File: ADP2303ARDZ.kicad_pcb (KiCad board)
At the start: 2 copper layers, 28 x 38 mm, 16 parts, among them P1 CONN_01X03, P2 CONN_01X03, U1 ADP230x, U2 MCP1825S

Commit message: rough layout
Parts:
- removed G***: LOGO, electronicSoup:LOGO
- added R2: R, footprints:R_0603_1608Metric, F.Cu at (144.6, 115.2)
- added R3: R, footprints:R_0603_1608Metric, F.Cu at (148.0, 115.2)
- C1, C2, C4, C6, C7: footprint Capacitors_SMD:C_0603_HandSoldering -> footprints:C_0603_1608Metric
- C3: value 0.1uF -> 0,1uF; footprint Capacitors_SMD:C_0603_HandSoldering -> footprints:C_0603_1608Metric
- C5: value C_Small -> C; footprint Capacitors_SMD:C_0603_HandSoldering -> footprints:C_0603_1608Metric
- D1: footprint Diodes_SMD:SMB_Standard -> footprints:D_SMB_Handsoldering
- L1: value 4.7uH -> VLF10040T; footprint electronicSoup:Inductor-VLF10040 -> footprints:L_TDK_VLF10040
- L2: value 3uH -> SRN6028; footprint electronicSoup:Inductor-SRN6028-Series -> footprints:L_Bourns-SRN6028
- P1: value CONN_01X03 -> Input; footprint Pin_Headers:Pin_Header_Straight_1x03 -> footprints:PinSocket_1x03_P2.54mm_Vertical
- P2: value CONN_01X03 -> Output; footprint Pin_Headers:Pin_Header_Straight_1x03 -> footprints:PinSocket_1x03_P2.54mm_Vertical
- R1: footprint Resistors_SMD:R_0603_HandSoldering -> footprints:R_0603_1608Metric
- U1: value ADP230x -> ADP2303ARDZ-5.0; footprint Housings_SOIC:SOIC-8-1EP_3.9x4.9mm_Pitch1.27mm -> footprints:SOIC-8-1EP_3.9x4.9mm_Pitch1.27mm
- U2: footprint TO_SOT_Packages_SMD:SOT-223 -> footprints:SOT-223
- moved L2 0.36 mm to (145.2, 83.9), turned to 0 degrees
- turned C1 to 90 degrees
- turned C2 to 90 degrees
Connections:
- net /3v3 renamed Net-(C7-Pad1)
- net /BST renamed Net-(C3-Pad1)
- net /SW renamed Net-(C3-Pad2)
- C1 pad 1: /Gnd -> Net-(C1-Pad1)
- C1 pad 2: /Vin -> Net-(C1-Pad2)
- C2 pad 1: /Gnd -> Net-(C1-Pad1)
- C2 pad 2: /Vin -> Net-(C1-Pad2)
- C4 pad 1: /5V -> Net-(C4-Pad1)
- C4 pad 2: /Gnd -> Net-(C1-Pad2)
- C5 pad 1: /5V -> Net-(C4-Pad1)
- C5 pad 2: /Gnd -> Net-(C1-Pad2)
- C6 pad 1: /5V -> Net-(C4-Pad1)
- C6 pad 2: /Gnd -> Net-(C1-Pad2)
- C7 pad 2: /Gnd -> Net-(C1-Pad2)
- D1 pad 2: /Gnd -> Net-(C1-Pad2)
- L1 pad 2: /5V -> Net-(C4-Pad1)
- L2 pad 2: /5V -> Net-(C4-Pad1)
- P1 pad 1: /Gnd -> Net-(C1-Pad2)
- P1 pad 2: /Vin -> Net-(C1-Pad1)
- P1 pad 3: /Gnd -> Net-(C1-Pad2)
- P2 pad 1: /Gnd -> Net-(C4-Pad1)
- P2 pad 3: /5V -> Net-(C1-Pad2)
- R1 pad 1: /Vin -> Net-(C1-Pad1)
- U1 pad 2: /Vin -> Net-(C1-Pad1)
- U1 pad 3: /Vin -> Net-(C1-Pad1)
- U1 pad 5: /5V -> Net-(R2-Pad1)
- U1 pad 6: (no net) -> Net-(U1-Pad6)
- U1 pad 7: /Gnd -> Net-(C1-Pad2)
- U1 pad 9: /Gnd -> Net-(C1-Pad2)
- U2 pad 1: /5V -> Net-(C4-Pad1)
- U2 pad 2: /Gnd -> Net-(C1-Pad2)
- U2 pad 4: /Gnd -> (no net)
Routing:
- net /Gnd: track 110.8 -> 0.00 mm
- net /5V: track 79.1 -> 0.00 mm, vias 1 -> 0
- net Net-(C3-Pad2): track 38.5 -> 3.32 mm
- net /Vin: track 19.9 -> 0.00 mm
- added copper zone on F.Cu, net /SW
- removed copper zone on B.Cu, net /Gnd
- removed copper zone on F.Cu, net Net-(C3-Pad2)

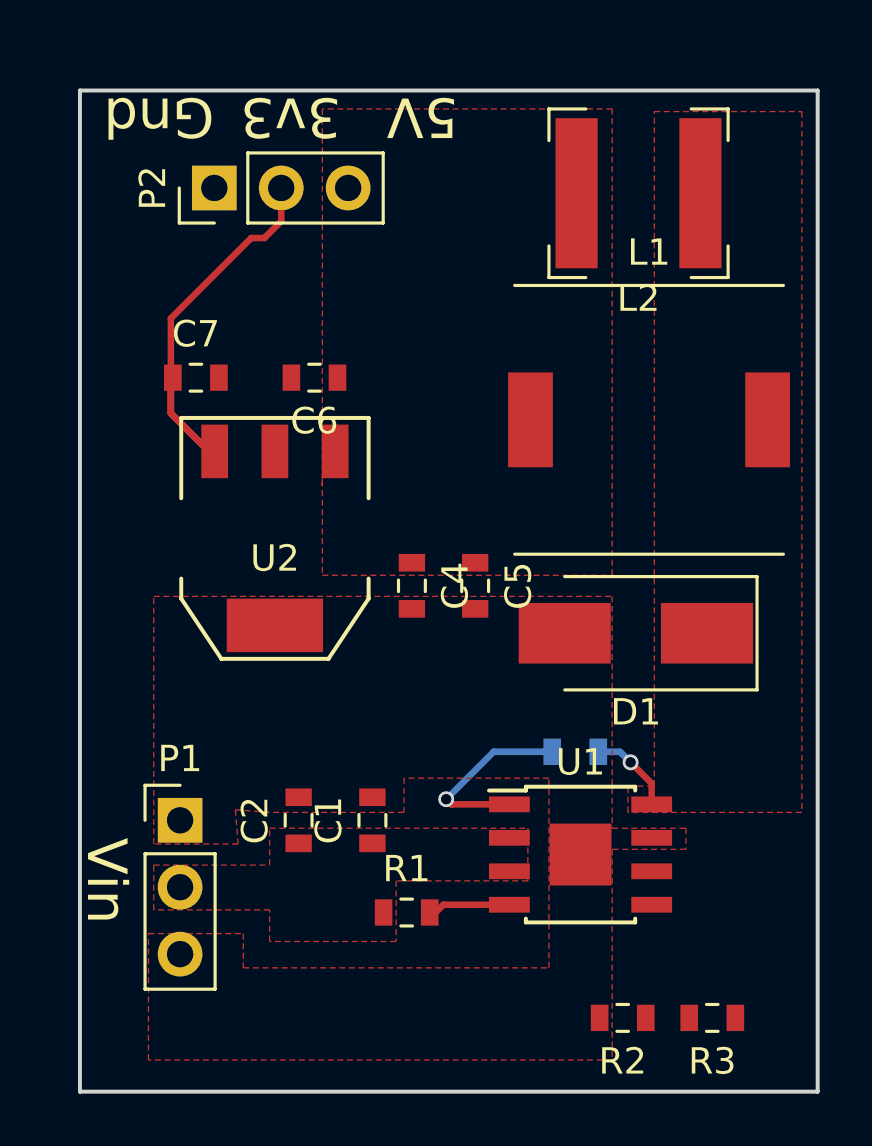
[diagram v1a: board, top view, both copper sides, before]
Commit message: corrected orientation of Inductors
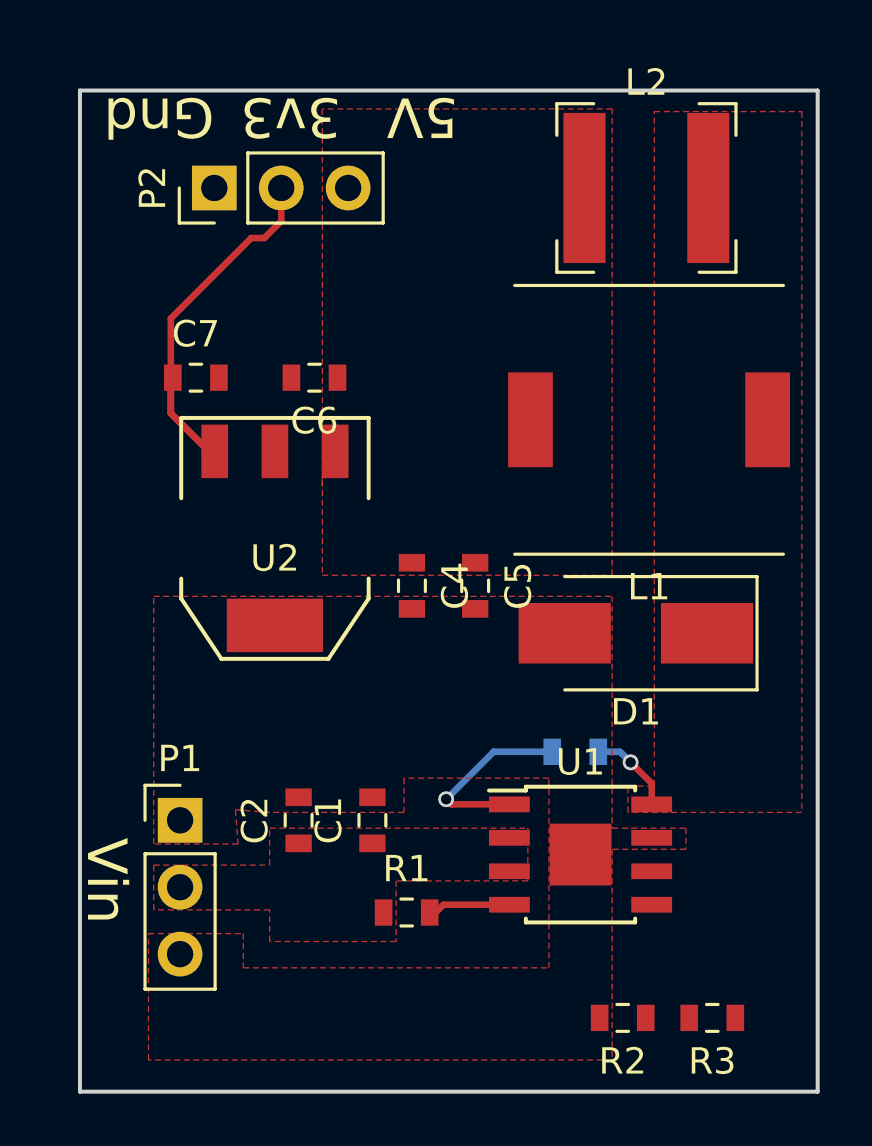
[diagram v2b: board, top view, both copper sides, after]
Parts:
- moved L2 0.36 mm to (145.5, 83.7), turned to 180 degrees
- turned L1 to 180 degrees
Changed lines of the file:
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@@
   )
   (module footprints:L_TDK_VLF10040 (layer F.Cu)
-    (at 145.6 92.5)
+    (at 145.6 92.5 180)
     (descr "Inductor,TDK, TDK-VLP-8040, 8.6mmx8.6mm")
     (tags "inductor TDK VLP smd VLF10040")
     (attr smd)
-    (fp_text reference L1 (at 0 -6.35) (layer F.SilkS)
+    (fp_text reference L1 (at 0 -6.35 180) (layer F.SilkS)
       (effects (font (size 1 1) (thickness 0.15)))
     )
-    (fp_text value VLF10040T (at 0 6) (layer F.Fab)
+    (fp_text value VLF10040T (at 0 6 180) (layer F.Fab)
       (effects (font (size 1 1) (thickness 0.15)))
     )
-    (fp_text user %R (at 0 0) (layer F.Fab)
+    (fp_text user %R (at 0 0 180) (layer F.Fab)
       (effects (font (size 1 1) (thickness 0.15)))
     )
@@
     (fp_line (start -5.1 -5.1) (end 5.1 -5.1) (layer F.SilkS) (width 0.12))
     (fp_circle (center 0 0) (end 3 3) (layer F.Fab) (width 0.1))
-    (pad 1 smd rect (at -4.5 0) (size 1.7 3.6) (layers F.Cu F.Paste F.Mask)
+    (pad 1 smd rect (at -4.5 0 180) (size 1.7 3.6) (layers F.Cu F.Paste F.Mask)
       (net 9 "Net-(C3-Pad2)"))
-    (pad 2 smd rect (at 4.5 0) (size 1.7 3.6) (layers F.Cu F.Paste F.Mask)
+    (pad 2 smd rect (at 4.5 0 180) (size 1.7 3.6) (layers F.Cu F.Paste F.Mask)
       (net 10 "Net-(C4-Pad1)"))
     (model ${KISYS3DMOD}/Inductor_SMD.3dshapes/L_TDK_VLF10040.wrl
@@
   )
   (module footprints:L_Bourns-SRN6028 (layer F.Cu)
-    (at 145.2 83.9)
+    (at 145.5 83.7 180)
     (descr "Bourns SRN6028 series SMD inductor")
     (tags "Bourns SRN6028 SMD inductor")
     (attr smd)
-    (fp_text reference L2 (at 0 4) (layer F.SilkS)
+    (fp_text reference L2 (at 0 4 180) (layer F.SilkS)
       (effects (font (size 1 1) (thickness 0.15)))
     )
-    (fp_text value SRN6028 (at 0 -4) (layer F.Fab)
+    (fp_text value SRN6028 (at 0 -4 180) (layer F.Fab)
       (effects (font (size 1 1) (thickness 0.15)))
     )
-    (fp_text user %R (at 0 0) (layer F.Fab)
+    (fp_text user %R (at 0 0 180) (layer F.Fab)
       (effects (font (size 1 1) (thickness 0.15)))
     )
@@
     (fp_line (start 3.3 3.1) (end -3.3 3.1) (layer F.CrtYd) (width 0.05))
     (fp_line (start -3.3 -3.1) (end -3.3 3.1) (layer F.CrtYd) (width 0.05))
-    (pad 1 smd rect (at -2.35 0) (size 1.6 5.7) (layers F.Cu F.Paste F.Mask)
+    (pad 1 smd rect (at -2.35 0 180) (size 1.6 5.7) (layers F.Cu F.Paste F.Mask)
       (net 9 "Net-(C3-Pad2)"))
-    (pad 2 smd rect (at 2.35 0) (size 1.6 5.7) (layers F.Cu F.Paste F.Mask)
+    (pad 2 smd rect (at 2.35 0 180) (size 1.6 5.7) (layers F.Cu F.Paste F.Mask)
       (net 10 "Net-(C4-Pad1)"))
     (model ${KISYS3DMOD}/Inductor_SMD.3dshapes/L_Bourns-SRN6028.wrl

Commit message: Fully connected but no Gnd plane as yet
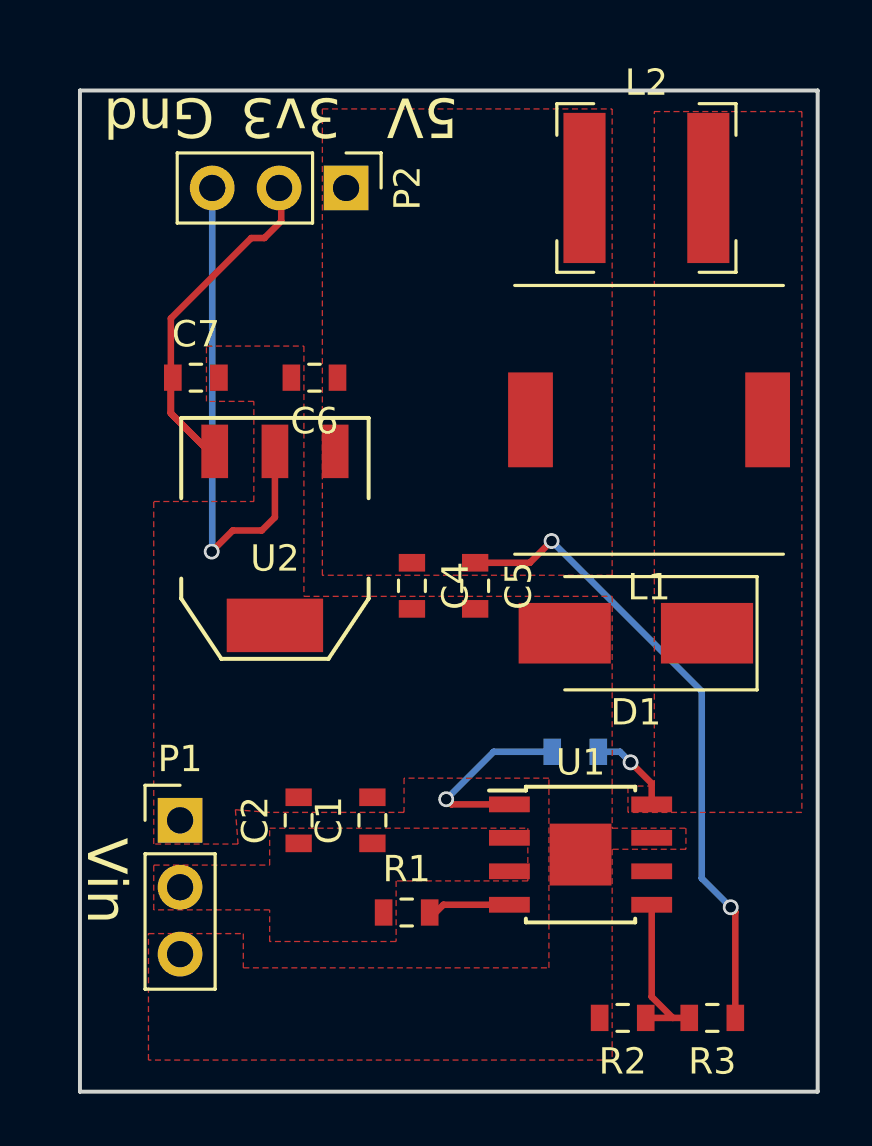
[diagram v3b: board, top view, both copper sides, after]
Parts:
- moved P2 5.00 mm to (134.1, 83.7), turned to 270 degrees
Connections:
- net Net-(C4-Pad1) renamed /5v
- net Net-(C7-Pad1) renamed /3v3
- C1 pad 1: Net-(C1-Pad1) -> /Vin
- C1 pad 2: Net-(C1-Pad2) -> /Gnd
- C2 pad 1: Net-(C1-Pad1) -> /Vin
- C2 pad 2: Net-(C1-Pad2) -> /Gnd
- C3 pad 2: Net-(C3-Pad2) -> /SW
- C4 pad 2: Net-(C1-Pad2) -> /Gnd
- C5 pad 2: Net-(C1-Pad2) -> /Gnd
- C6 pad 2: Net-(C1-Pad2) -> /Gnd
- C7 pad 2: Net-(C1-Pad2) -> /Gnd
- D1 pad 1: Net-(C3-Pad2) -> /SW
- D1 pad 2: Net-(C1-Pad2) -> /Gnd
- L1 pad 1: Net-(C3-Pad2) -> /SW
- L2 pad 1: Net-(C3-Pad2) -> /SW
- P1 pad 1: Net-(C1-Pad2) -> /Gnd
- P1 pad 2: Net-(C1-Pad1) -> /Vin
- P1 pad 3: Net-(C1-Pad2) -> /Gnd
- P2 pad 3: Net-(C1-Pad2) -> /Gnd
- R1 pad 1: Net-(C1-Pad1) -> /Vin
- R2 pad 2: Net-(C1-Pad2) -> /Gnd
- U1 pad 2: Net-(C1-Pad1) -> /Vin
- U1 pad 3: Net-(C1-Pad1) -> /Vin
- U1 pad 6: Net-(U1-Pad6) -> (no net)
- U1 pad 7: Net-(C1-Pad2) -> /Gnd
- U1 pad 8: Net-(C3-Pad2) -> /SW
- U1 pad 9: Net-(C1-Pad2) -> /Gnd
- U2 pad 2: Net-(C1-Pad2) -> /Gnd
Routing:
- net /5v: track 0.00 -> 24.2 mm, vias 0 -> 2
- net /Gnd: track 0.00 -> 19.2 mm, vias 0 -> 1
- net Net-(R2-Pad1): track 0.00 -> 6.28 mm
- net Net-(C3-Pad2): track 3.32 -> 0.00 mm, vias 1 -> 0
- net /SW: track 0.00 -> 3.32 mm, vias 0 -> 1
- added copper zone on F.Cu, net /5v
- removed copper zone on F.Cu, net /5V

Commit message: Added 0805 Cap Footprint
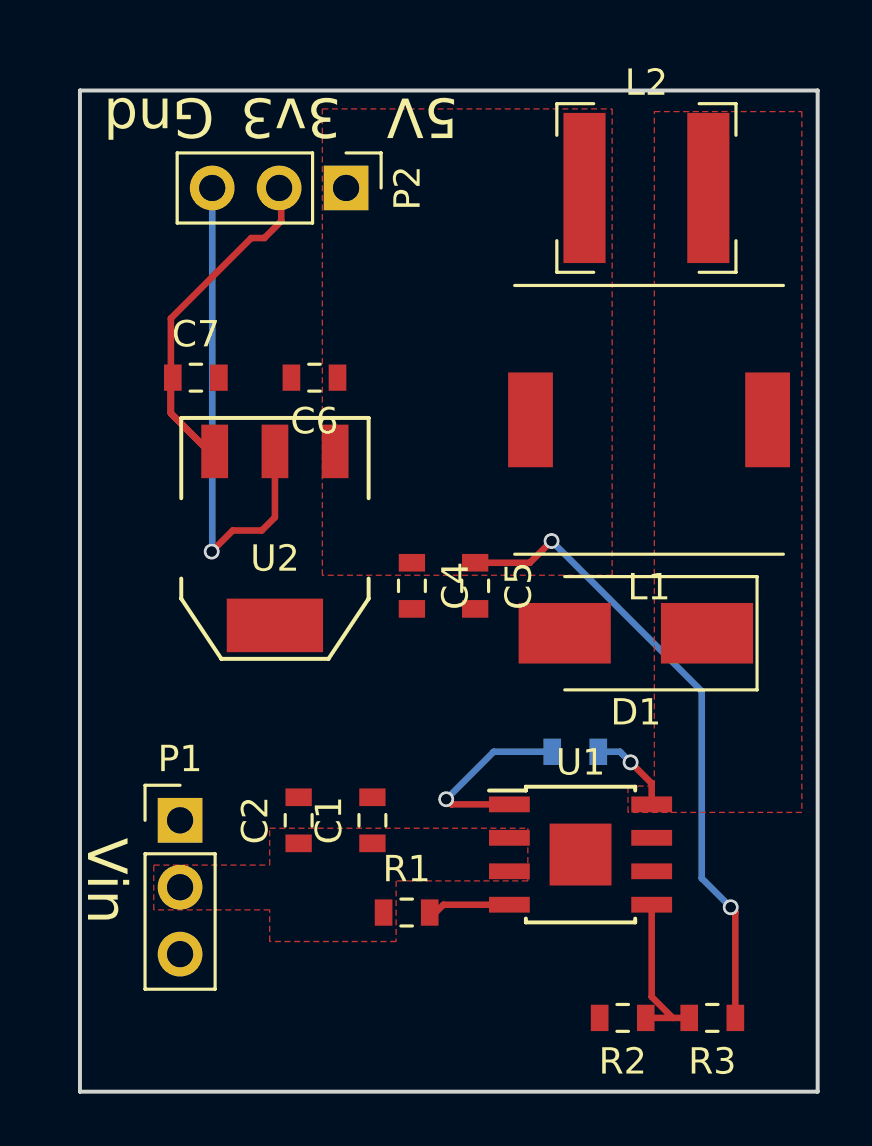
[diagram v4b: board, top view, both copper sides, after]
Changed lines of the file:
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@@
   (segment (start 131.64 84.96) (end 131.64 83.7) (width 0.25) (layer F.Cu) (net 8) (status 20))
   (zone (net 2) (net_name /Vin) (layer F.Cu) (hatch edge 0.508)
+    (priority 2)
     (connect_pads (clearance 0.508))
     (min_thickness 0.254)
@@
   )
   (zone (net 4) (net_name /SW) (layer F.Cu) (hatch edge 0.508)
+    (priority 2)
     (connect_pads (clearance 0.508))
     (min_thickness 0.254)
@@
   )
   (zone (net 7) (net_name /5v) (layer F.Cu) (hatch edge 0.508)
+    (priority 2)
     (connect_pads (clearance 0.508))
     (min_thickness 0.254)
@@
     (polygon
       (pts
-        (xy 132.5 99.2) (xy 144.2 99.2) (xy 144.2 108) (xy 147 108) (xy 147 108.8)
-        (xy 144.2 108.8) (xy 144.2 116.8) (xy 126.6 116.8) (xy 126.6 112) (xy 130.2 112)
-        (xy 130.2 113.3) (xy 141.8 113.3) (xy 141.8 106.1) (xy 136.3 106.1) (xy 136.3 107.4)
-        (xy 131.2 107.4) (xy 129.9 107.3) (xy 130 108.6) (xy 126.8 108.6) (xy 126.8 95.6)
-        (xy 130.6 95.6) (xy 130.6 91.8) (xy 128.8 91.8) (xy 128.8 89.7) (xy 132.5 89.7)
+        (xy 152 118) (xy 124 118) (xy 124 80) (xy 152 80)
       )
     )

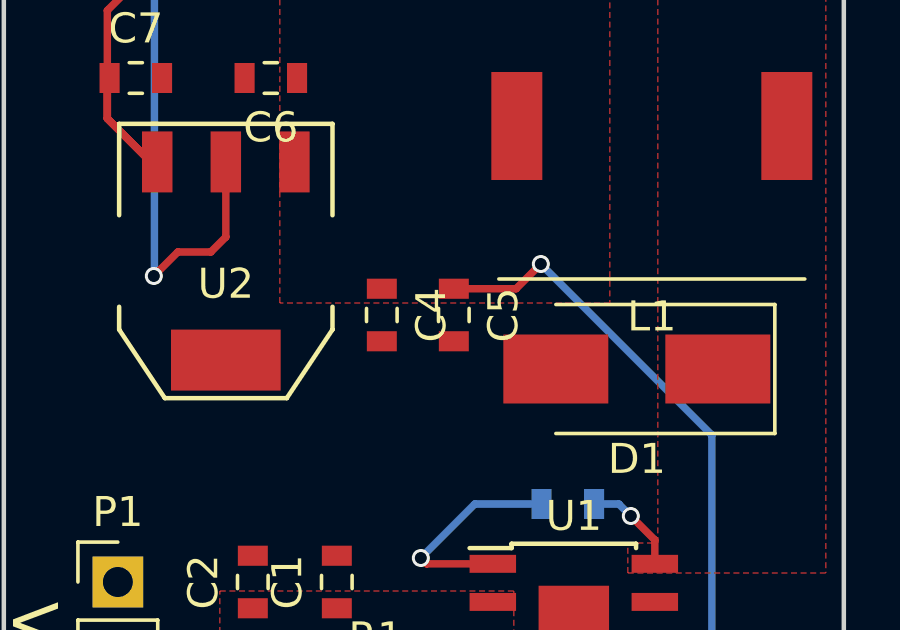
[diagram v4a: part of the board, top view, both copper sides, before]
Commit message: Change layout to use 0805 Cap
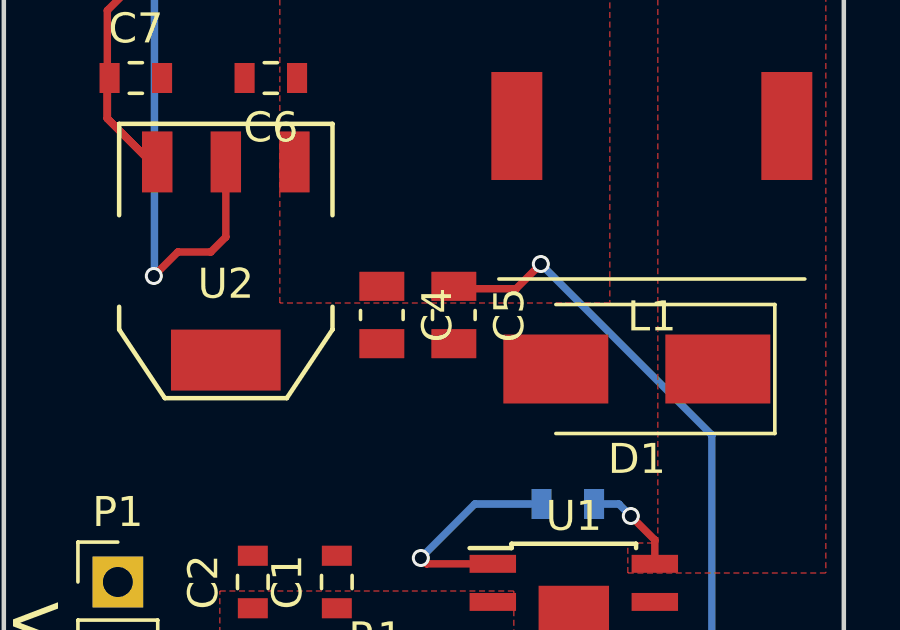
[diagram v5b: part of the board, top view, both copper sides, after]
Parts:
- C4, C5: footprint footprints:C_0603_1608Metric -> footprints:C_0805_2012Metric
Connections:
- U1 pad 6: (no net) -> Net-(U1-Pad6)
